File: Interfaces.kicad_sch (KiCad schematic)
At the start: 15 parts, among them J14 I2C1_Headers, J15 SPI1_Headers, J16 General_Pin_Header, J3 LPUART1_Headers, J8 Debug_Pins

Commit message: Update
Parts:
- removed J14: I2C1_Headers, Connector_PinHeader_2.54mm:PinHeader_2x03_P2.54mm_Horizontal, symbol Connector_Generic:Conn_02x03_Odd_Even
- removed J15: SPI1_Headers, Connector_PinHeader_2.54mm:PinHeader_2x03_P2.54mm_Horizontal, symbol Connector_Generic:Conn_02x03_Odd_Even
- removed J16: General_Pin_Header, Connector_PinHeader_2.54mm:PinHeader_2x03_P2.54mm_Horizontal, symbol Connector_Generic:Conn_02x03_Odd_Even
- removed J3: LPUART1_Headers, Connector_PinHeader_2.54mm:PinHeader_2x03_P2.54mm_Horizontal, symbol Connector_Generic:Conn_02x03_Odd_Even
- removed J8: Debug_Pins, Connector_PinHeader_2.54mm:PinHeader_2x04_P2.54mm_Horizontal, symbol Connector_Generic:Conn_02x04_Odd_Even
- removed R10, R11, R15, R19, R7: 33R, Resistor_SMD:R_0805_2012Metric, symbol Device:R
- added C1: 1uF, Capacitor_SMD:C_0805_2012Metric, symbol Device:C
- added DI1: Diode_PESD5V0U2BT-Q, Package_TO_SOT_SMD:SOT-23, symbol Personal_Projects:Diode_PESD5V0U2BT-Q
- added FPC1: FPC_0545481072, Personal_Project:FPC_0545481072, symbol Personal_Projects:FPC_0545481072
- added J2: UART1_HDR, Connector_PinHeader_2.54mm:PinHeader_2x03_P2.54mm_Horizontal, symbol Connector_Generic:Conn_02x03_Odd_Even
- added J3: SWDB, Connector_PinHeader_2.54mm:PinHeader_2x04_P2.54mm_Horizontal, symbol Connector_Generic:Conn_02x04_Odd_Even
- added J5: I/O_HDR, symbol Connector_Generic:Conn_02x06_Odd_Even
- added J7: I2C2_Headers, Connector_PinHeader_2.54mm:PinHeader_2x03_P2.54mm_Horizontal, symbol Connector_Generic:Conn_02x03_Odd_Even
- added J9: I2C1_Headers, Connector_PinHeader_2.54mm:PinHeader_2x03_P2.54mm_Horizontal, symbol Connector_Generic:Conn_02x03_Odd_Even
- added R14: 33R, Resistor_SMD:R_0805_2012Metric, symbol Device:R
- added R18, R20, R21, R22: 10k, Resistor_SMD:R_0805_2012Metric, symbol Device:R
- added SHLD1: RFShield_OnePiece, Personal_Project:RF_Shield_MS631-10F, symbol Device:RFShield_OnePiece
- added U2: ~, Personal_Project:Button_KMR231GLFS, symbol Personal_Projects:Button_KMR231GLFS
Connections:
- net GND: now also C1.1, DI1.3 (CC), FPC1.1, FPC1.10, FPC1.11 (MP1), FPC1.12 (MP2), FPC1.3, FPC1.5, FPC1.6, FPC1.8, J2.1 (Pin_1), J2.2 (Pin_2), J2.4 (Pin_4), J2.5 (Pin_5), J2.6 (Pin_6), J3.1 (Pin_1), J3.3 (Pin_3), J3.5 (Pin_5), J3.7 (Pin_7), J5.1 (Pin_1), J5.11 (Pin_11), J5.3 (Pin_3), J5.5 (Pin_5), J5.7 (Pin_7), J5.9 (Pin_9), J7.2 (Pin_2), J7.3 (Pin_3), J7.4 (Pin_4), J7.6 (Pin_6), J9.2 (Pin_2), J9.3 (Pin_3), J9.4 (Pin_4), J9.6 (Pin_6), SHLD1.1 (Shield), U2.3, U2.4, U2.5 (GND)
- net NRST: now also J3.6 (Pin_6)
- net PB7_I2C1_SDA renamed I2C1_SDA_HDR
- net I2C1_SDA_HDR: now also J9.1 (Pin_1), R21.2
- net PB8_I2C1_SCL renamed I2C1_SCL_HDR
- net I2C1_SCL_HDR: now also J9.5 (Pin_5), R22.2
- new net: J2.3 (Pin_3), R14.2
- new net +3.3V: R18.1, R20.1, R21.1, R22.1
- new net I2C2_SCL_HDR: DI1.2 (K2), J7.5 (Pin_5), R20.2
- new net I2C2_SDA_HDR: DI1.1 (K1), J7.1 (Pin_1), R18.2
- new net I/O_HDR0: J5.2 (Pin_2)
- new net I/O_HDR1: J5.4 (Pin_4)
- new net I/O_HDR2: J5.6 (Pin_6)
- new net I/O_HDR3: J5.8 (Pin_8)
- new net I/O_HDR4: J5.10 (Pin_10)
- new net I/O_HDR5: J5.12 (Pin_12)
- new net SPI_CLK: FPC1.7
- new net SPI_CS: FPC1.9
- new net SPI_MISO: FPC1.4
- new net SPI_MOSI: FPC1.2
- new net SWCLK: J3.2 (Pin_2)
- new net SWDIO: J3.8 (Pin_8)
- new net SWO: J3.4 (Pin_4)
- new net UART1_TX/RX: R14.1
- new net USR_BTN: C1.2, U2.1, U2.2
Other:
- note added: "Place ESD close to the header"
- note removed: "Chip Select pin on general pin header"
- moved on the sheet: H5, H6, H7, H8

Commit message: Update
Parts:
- J5: footprint (none) -> Connector_PinHeader_2.54mm:PinHeader_2x06_P2.54mm_Vertical
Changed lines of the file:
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@@
 			)
 		)
-		(property "Footprint" ""
+		(property "Footprint" "Connector_PinHeader_2.54mm:PinHeader_2x06_P2.54mm_Vertical"
 			(at 133.35 66.04 0)
 			(effects

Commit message: Update
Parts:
- J5: footprint Connector_PinHeader_2.54mm:PinHeader_2x06_P2.54mm_Vertical -> Connector_PinHeader_2.54mm:PinHeader_2x06_P2.54mm_Horizontal
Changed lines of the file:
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@@
 			)
 		)
-		(property "Footprint" "Connector_PinHeader_2.54mm:PinHeader_2x06_P2.54mm_Vertical"
+		(property "Footprint" "Connector_PinHeader_2.54mm:PinHeader_2x06_P2.54mm_Horizontal"
 			(at 133.35 66.04 0)
 			(effects

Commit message: Update
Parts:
- removed J5: I/O_HDR, Connector_PinHeader_2.54mm:PinHeader_2x06_P2.54mm_Horizontal, symbol Connector_Generic:Conn_02x06_Odd_Even
- added J1: I/O_HDR, Connector_PinHeader_2.54mm:PinHeader_2x03_P2.54mm_Horizontal, symbol Connector_Generic:Conn_02x03_Odd_Even
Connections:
- net +3.3V: now also J1.1 (Pin_1)
- net GND: now also J1.3 (Pin_3), J1.5 (Pin_5)
- net I/O_HDR0: now also J1.2 (Pin_2)
- net I/O_HDR1: now also J1.4 (Pin_4)
- net I/O_HDR2: now also J1.6 (Pin_6)
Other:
- moved on the sheet: H5, H6, H7, H8, J3

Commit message: Update
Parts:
- removed FPC1: FPC_0545481072, Personal_Project:FPC_0545481072, symbol Personal_Projects:FPC_0545481072
- added FPC1: FPC_10051922-1010ELF, Personal_Project:FPC_10051922_1010, symbol Personal_Projects:FPC_10051922-1010ELF
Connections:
- net GND: now also FPC1.1, FPC1.10, FPC1.11 (MP1), FPC1.12 (MP2), FPC1.3, FPC1.5, FPC1.6, FPC1.8
- net SPI_CLK: now also FPC1.7
- net SPI_CS: now also FPC1.9
- net SPI_MISO: now also FPC1.4
- net SPI_MOSI: now also FPC1.2
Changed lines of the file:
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@@
 	)
 	(symbol
-		(lib_id "Personal_Projects:FPC_0545481072")
+		(lib_id "Personal_Projects:FPC_10051922-1010ELF")
 		(at 43.18 43.18 0)
 		(unit 1)
@@
 		(dnp no)
 		(property "Reference" "FPC1"
-			(at 43.18 33.782 0)
+			(at 54.61 26.924 0)
 			(effects
 				(font
-					(size 1.27 1.27)
+					(size 1.524 1.524)
 				)
 				(justify right)
 			)
 		)
-		(property "Value" "FPC_0545481072"
-			(at 43.18 36.322 0)
+		(property "Value" "FPC_10051922-1010ELF"
+			(at 77.47 29.718 0)
 			(effects
 				(font
-					(size 1.27 1.27)
+					(size 1.524 1.524)
 				)
 				(justify right)
 			)
 		)
-		(property "Footprint" "Personal_Project:FPC_0545481072"
-			(at 64.77 138.1 0)
+		(property "Footprint" "Personal_Project:FPC_10051922_1010"
+			(at 43.18 90.17 0)
 			(effects
 				(font
 					(size 1.27 1.27)
+					(italic yes)
 				)
-				(justify left top)
 				(hide yes)
 			)
 		)
-		(property "Datasheet" "https://www.molex.com/en-us/products/part-detail-pdf/545481072?display=pdf"
-			(at 64.77 238.1 0)
+		(property "Datasheet" "10051922-1010ELF"
+			(at 43.18 86.36 0)
 			(effects
 				(font
 					(size 1.27 1.27)
+					(italic yes)
 				)
-				(justify left top)
 				(hide yes)
 			)
 		)
-		(property "Description" "0.50mm Pitch Easy-On FFC/FPC Connector, 1.20mm Height, Right-Angle, Surface Mount, ZIF, Bottom Contact Style, 10 Circuits, Gold (Au) Plating"
-			(at 43.18 73.66 0)
+		(property "Description" ""
+			(at 55.88 43.18 0)
 			(effects
 				(font
@@
 			)
 		)
-		(property "Height" "1.3"
-			(at 64.77 438.1 0)
-			(effects
-				(font
-					(size 1.27 1.27)
-				)
-				(justify left top)
-				(hide yes)
-			)
+		(pin "6"
 		)
-		(property "Arrow Part Number" "0545481072"
-			(at 64.77 538.1 0)
-			(effects
-				(font
-					(size 1.27 1.27)
-				)
-				(justify left top)
-				(hide yes)
-			)
-		)
-		(property "Arrow Price/Stock" ""
-			(at 64.77 638.1 0)
-			(effects
-				(font
-					(size 1.27 1.27)
-				)
-				(justify left top)
-				(hide yes)
-			)
-		)
-		(property "Manufacturer_Name" "Molex"
-			(at 64.77 738.1 0)
-			(effects
-				(font
-					(size 1.27 1.27)
-				)
-				(justify left top)
-				(hide yes)
-			)
-		)
-		(property "Manufacturer_Part_Number" "0545481072"
-			(at 64.77 838.1 0)
-			(effects
-				(font
-					(size 1.27 1.27)
-				)
-				(justify left top)
-				(hide yes)
-			)
+		(pin "9"
 		)
 		(pin "4"
@@
 		(pin "7"
 		)
-		(pin "6"
+		(pin "2"
 		)
 		(pin "5"
 		)
-		(pin "2"
+		(pin "3"
 		)
 		(pin "8"
 		)
-		(pin "3"
+		(pin "12"
 		)
 		(pin "10"
 		)
-		(pin "12"
+		(pin "1"
 		)
 		(pin "11"
 		)
-		(pin "9"
-		)
-		(pin "1"
-		)
 		(instances
-			(project "LoRa_Board"
+			(project ""
 				(path "/34ccaf76-212c-4f8e-9afa-bb7eea5015e3/336ebea6-c9a7-4c8d-a774-b509fb11d0ab"
 					(reference "FPC1")

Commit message: Update Readme file
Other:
- company: (none) -> Peter Hancak
- title: (none) -> LoRa Board
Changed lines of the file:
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@@
 	(generator_version "8.0")
 	(paper "USLetter")
+	(title_block
+		(title "LoRa Board")
+		(date "2026-03-17")
+		(rev "B")
+		(company "Peter Hancak")
+	)
 	(junction
 		(at 217.17 121.92)

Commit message: Update
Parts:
- U2: value ~ -> (none)

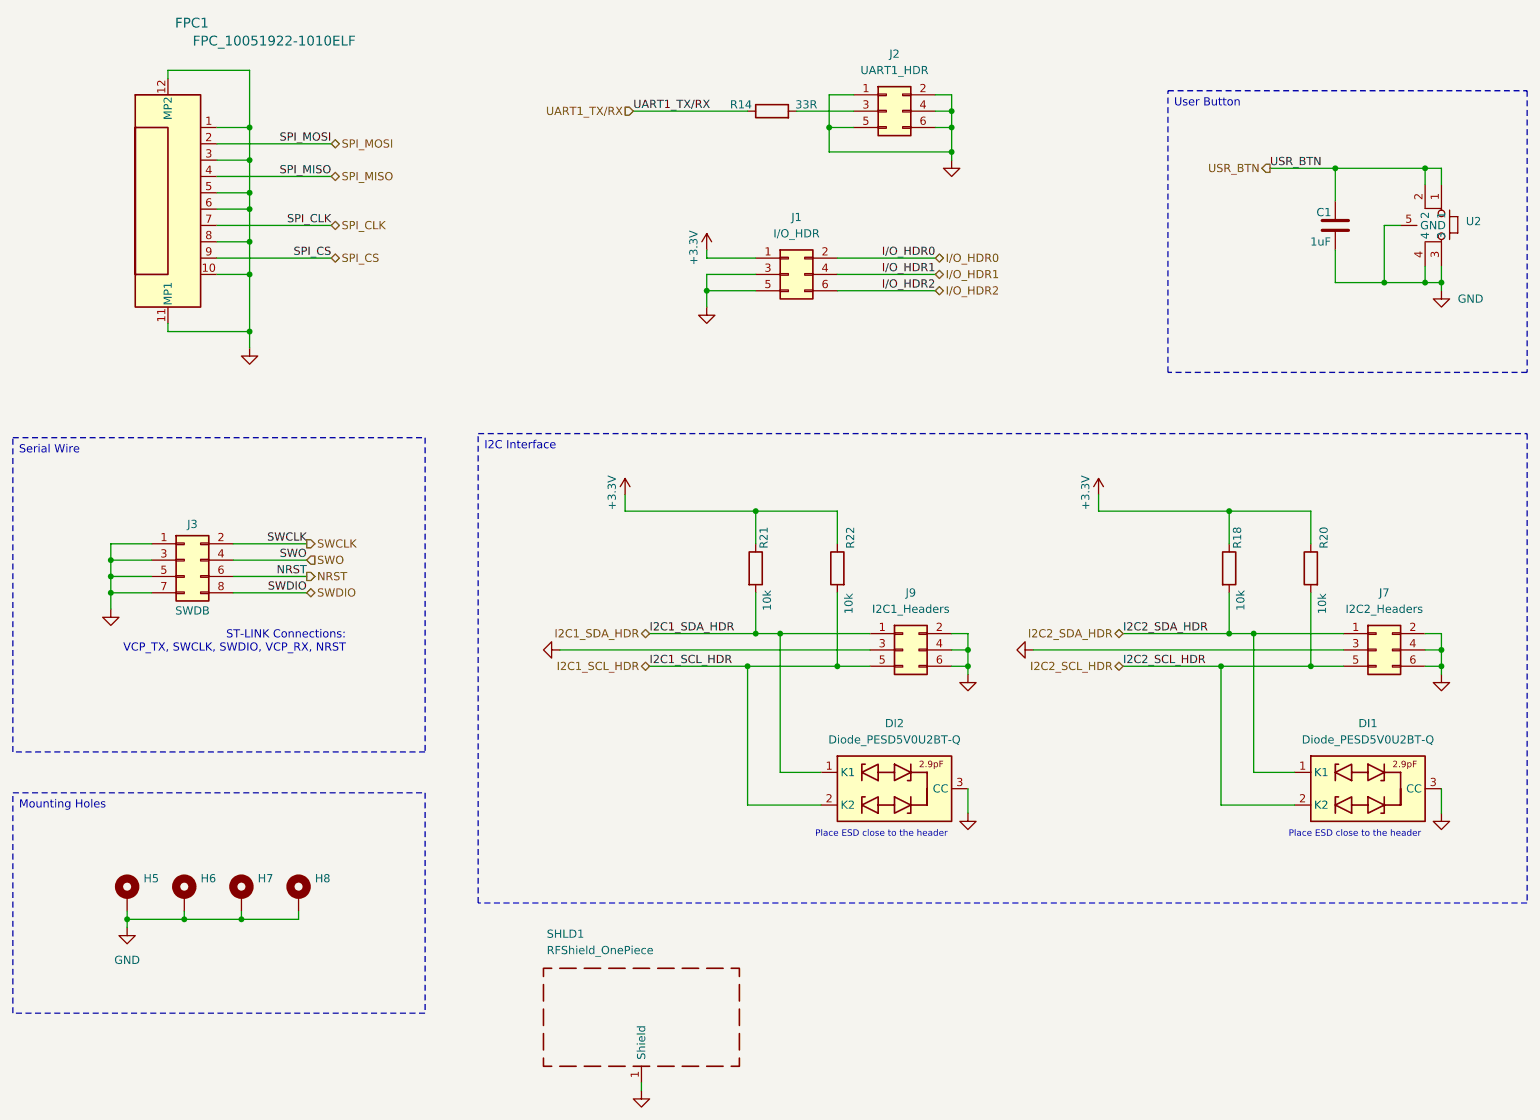
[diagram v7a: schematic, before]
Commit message: Schematics Update
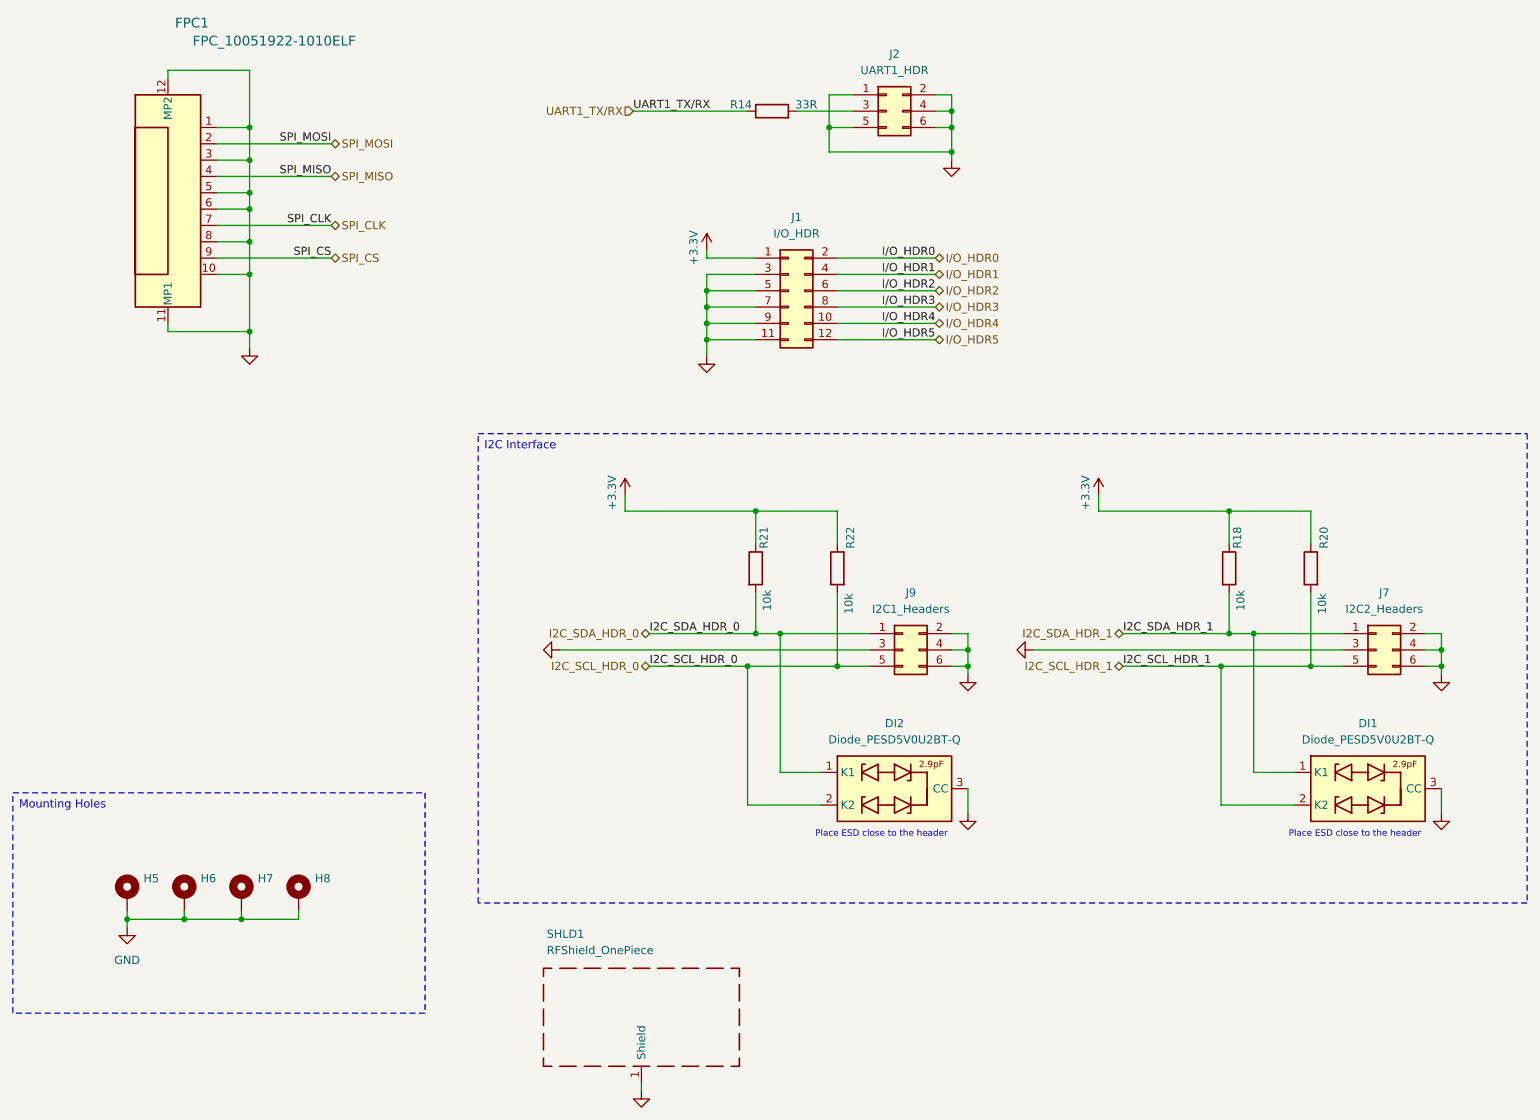
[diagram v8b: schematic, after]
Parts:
- removed C1: 1uF, Capacitor_SMD:C_0805_2012Metric, symbol Device:C
- removed J1: I/O_HDR, Connector_PinHeader_2.54mm:PinHeader_2x03_P2.54mm_Horizontal, symbol Connector_Generic:Conn_02x03_Odd_Even
- removed J3: SWDB, Connector_PinHeader_2.54mm:PinHeader_2x04_P2.54mm_Horizontal, symbol Connector_Generic:Conn_02x04_Odd_Even
- removed U2: (no value), Personal_Project:Button_KMR231GLFS, symbol Personal_Projects:Button_KMR231GLFS
- added J1: I/O_HDR, symbol Connector_Generic:Conn_02x06_Odd_Even
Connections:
- net +3.3V: now also J1.1 (Pin_1)
- net GND: now also J1.11 (Pin_11), J1.3 (Pin_3), J1.5 (Pin_5), J1.7 (Pin_7), J1.9 (Pin_9)
- net I/O_HDR0: now also J1.2 (Pin_2)
- net I/O_HDR1: now also J1.4 (Pin_4)
- net I/O_HDR2: now also J1.6 (Pin_6)
- net I2C1_SCL_HDR renamed I2C_SCL_HDR_0
- net I2C1_SDA_HDR renamed I2C_SDA_HDR_0
- net I2C2_SCL_HDR renamed I2C_SCL_HDR_1
- net I2C2_SDA_HDR renamed I2C_SDA_HDR_1
- new net I/O_HDR3: J1.8 (Pin_8)
- new net I/O_HDR4: J1.10 (Pin_10)
- new net I/O_HDR5: J1.12 (Pin_12)
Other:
- note removed: "ST-LINK Connections: VCP_TX, SWCLK, SWDIO, VCP_RX, NRST"
- title: LoRa Board -> LoRa STM32WL55CCU6 Board
